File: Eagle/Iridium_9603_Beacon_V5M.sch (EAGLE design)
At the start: 103 parts, among them CON4 uFL, J1 SS4-10-3.50-X-D, Q1 DMG3415U-7, Q2 DMG3415U-7, Q3 DMG3415U-7, Q4 DMG3415U-7, Q5 2N2222, U1 MCP111T-240E/TT, U2 SPX3819-3.3, U3 LTC3225EDDB#TRMPBF, U4 MPL3115A2LGA8, U5 ATSAMD21G18_QFN, U6 MAX-M8, U7 LT1634-1,25BMCMS8, X1 32.768

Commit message: nr
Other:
- note added: "V5M: Double AA battery capacity Added mounting holes (M3)"
- note removed: "V5M: Double AA battery capacity"
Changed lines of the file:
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@@
 Added a pad for a battery power switch</text>
 <text x="157.48" y="149.86" size="2.54" layer="91" align="top-left">V5M:
-Double AA battery capacity</text>
+Double AA battery capacity
+Added mounting holes (M3)</text>
 </plain>
 <instances>

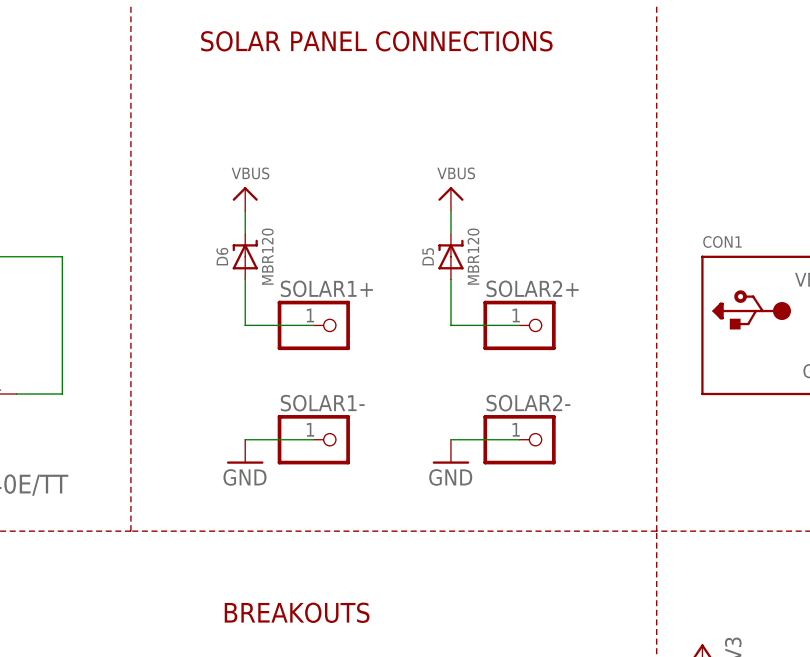
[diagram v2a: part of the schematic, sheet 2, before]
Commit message: removing backup eagle files, edits to V5M PCB board
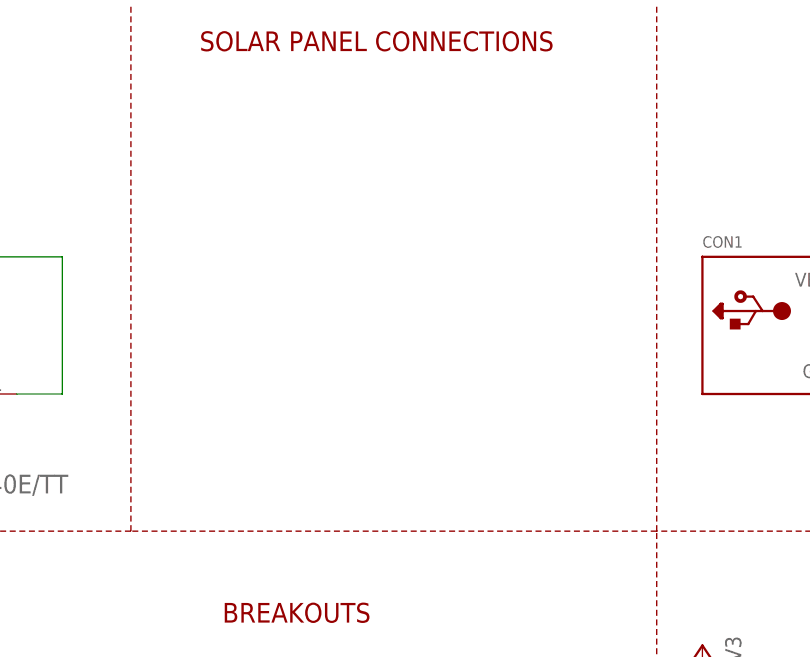
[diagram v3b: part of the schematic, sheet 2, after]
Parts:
- removed D5, D6: MBR120, microbuilder:DIODE-SCHOTTKYSOD-123
- removed SOLAR1+, SOLAR1-, SOLAR2+, SOLAR2-: (no value), adafruit:PINHD-1X1
- added FD3: FIDUCIAL1X2, SparkFun-Aesthetics:FIDUCIAL1X2
- added U$53: 7101K2AV2QE, argol-eagle-library:7101K2AV2QE
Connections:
- removed net N$14: D5.A, SOLAR2+.1
- removed net N$4: D6.A, SOLAR1+.1
- net GND: now also U$53.P$1; no longer SOLAR1-.1, SOLAR2-.1
- net N$15: now also U$53.P$2
- net VBUS: no longer D5.C, D6.C
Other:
- note added: "V5M: Double AA battery capacity Added mounting holes (M3) Added SPDT Switch for power Removed Solar Power connections"
- note removed: "Cut link if installing power switch"
- note removed: "V5M: Double AA battery capacity Added mounting holes (M3)"
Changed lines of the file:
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@@
 <layer number="59" name="tCarbon" color="7" fill="1" visible="no" active="no"/>
 <layer number="60" name="bCarbon" color="7" fill="1" visible="no" active="no"/>
+<layer number="88" name="SimResults" color="9" fill="1" visible="yes" active="yes"/>
+<layer number="89" name="SimProbes" color="9" fill="1" visible="yes" active="yes"/>
 <layer number="90" name="Modules" color="5" fill="1" visible="yes" active="yes"/>
 <layer number="91" name="Nets" color="2" fill="1" visible="yes" active="yes"/>
@@
 <part name="D3" library="microbuilder" deviceset="DIODE-SCHOTTKY" device="SOD-123" value="MBR120"/>
 <part name="D2" library="microbuilder" deviceset="DIODE-SCHOTTKY" device="SOD-123" value="MBR120"/>
-<part name="SOLAR1-" library="adafruit" library_urn="urn:adsk.eagle:library:420" deviceset="PINHD-1X1" device="" package3d_urn="urn:adsk.eagle:package:6240654/1"/>
-<part name="SOLAR2-" library="adafruit" library_urn="urn:adsk.eagle:library:420" deviceset="PINHD-1X1" device="" package3d_urn="urn:adsk.eagle:package:6240654/1"/>
-<part name="SOLAR1+" library="adafruit" library_urn="urn:adsk.eagle:library:420" deviceset="PINHD-1X1" device="" package3d_urn="urn:adsk.eagle:package:6240654/1"/>
-<part name="SOLAR2+" library="adafruit" library_urn="urn:adsk.eagle:library:420" deviceset="PINHD-1X1" device="" package3d_urn="urn:adsk.eagle:package:6240654/1"/>
-<part name="GND5" library="supply1" library_urn="urn:adsk.eagle:library:371" deviceset="GND" device=""/>
-<part name="GND6" library="supply1" library_urn="urn:adsk.eagle:library:371" deviceset="GND" device=""/>
-<part name="U$34" library="microbuilder" deviceset="VBUS" device=""/>
-<part name="D5" library="microbuilder" deviceset="DIODE-SCHOTTKY" device="SOD-123" value="MBR120"/>
-<part name="D6" library="microbuilder" deviceset="DIODE-SCHOTTKY" device="SOD-123" value="MBR120"/>
-<part name="U$2" library="microbuilder" deviceset="VBUS" device=""/>
 <part name="Q4" library="microbuilder" deviceset="MOSFET-P" device="WIDE" value="DMG3415U-7 "/>
 <part name="Q5" library="transistor" library_urn="urn:adsk.eagle:library:402" deviceset="*-NPN-" device="SOT23-BEC" package3d_urn="urn:adsk.eagle:package:28748/2" technology="MMBT2222ALT1" value="2N2222"/>
@@
 <part name="BAT5" library="SparkFun-Electromechanical" deviceset="BATTERY" device="KEYSTONE92"/>
 <part name="BAT6" library="SparkFun-Electromechanical" deviceset="BATTERY" device="KEYSTONE92"/>
+<part name="U$53" library="argol-eagle-library" deviceset="7101K2AV2QE" device=""/>
+<part name="FD3" library="SparkFun-Aesthetics" deviceset="FIDUCIAL" device="1X2"/>
 </parts>
 <sheets>
@@
 <text x="228.092" y="65.024" size="1.778" layer="91" align="bottom-center">Pads for battery
 power switch</text>
-<text x="189.484" y="64.516" size="1.778" layer="91" align="bottom-center">Cut link if installing
-power switch</text>
-<wire x1="207.772" y1="71.882" x2="205.232" y2="71.882" width="0.1524" layer="150"/>
-<wire x1="205.232" y1="71.882" x2="205.232" y2="61.722" width="0.1524" layer="150"/>
-<wire x1="205.232" y1="61.722" x2="207.772" y2="61.722" width="0.1524" layer="150"/>
 </plain>
 <instances>
@@
 <attribute name="VALUE" x="229.87" y="85.09" size="1.778" layer="96" rot="R270"/>
 </instance>
+<instance part="U$53" gate="G$1" x="193.04" y="71.12" smashed="yes" rot="R180"/>
+<instance part="FD3" gate="G$1" x="231.14" y="35.56" smashed="yes"/>
 </instances>
 <busses>
@@
 <segment>
 <pinref part="U$43" gate="G$1" pin="GND"/>
+<wire x1="218.44" y1="61.722" x2="218.44" y2="55.88" width="0.1524" layer="91"/>
 <pinref part="GND" gate="G$1" pin="1"/>
 <wire x1="210.312" y1="61.722" x2="218.44" y2="61.722" width="0.1524" layer="91"/>
-<wire x1="218.44" y1="61.722" x2="218.44" y2="55.88" width="0.1524" layer="91"/>
+<pinref part="U$53" gate="G$1" pin="P$1"/>
+<wire x1="180.34" y1="66.04" x2="180.34" y2="61.722" width="0.1524" layer="91"/>
+<wire x1="180.34" y1="61.722" x2="210.312" y2="61.722" width="0.1524" layer="91"/>
+<junction x="210.312" y="61.722"/>
 </segment>
 </net>
@@
 <wire x1="236.22" y1="76.2" x2="218.44" y2="76.2" width="0.1524" layer="91"/>
 <junction x="218.44" y="76.2"/>
+<junction x="210.312" y="71.882"/>
+<pinref part="U$53" gate="G$1" pin="P$2"/>
+<wire x1="210.312" y1="71.882" x2="210.312" y2="71.12" width="0.1524" layer="91"/>
+<wire x1="210.312" y1="71.12" x2="198.12" y2="71.12" width="0.1524" layer="91"/>
 </segment>
 </net>
@@
 <attribute name="VALUE" x="30.48" y="142.24" size="1.016" layer="96" font="vector" ratio="15" rot="R90" align="center"/>
 </instance>
-<instance part="SOLAR1-" gate="G$1" x="180.34" y="127" smashed="yes">
-<attribute name="NAME" x="173.99" y="130.175" size="1.778" layer="95"/>
-<attribute name="VALUE" x="173.99" y="121.92" size="1.778" layer="96"/>
-</instance>
-<instance part="SOLAR2-" gate="G$1" x="203.2" y="127" smashed="yes">
-<attribute name="NAME" x="196.85" y="130.175" size="1.778" layer="95"/>
-<attribute name="VALUE" x="196.85" y="121.92" size="1.778" layer="96"/>
-</instance>
-<instance part="SOLAR1+" gate="G$1" x="180.34" y="139.7" smashed="yes">
-<attribute name="NAME" x="173.99" y="142.875" size="1.778" layer="95"/>
-<attribute name="VALUE" x="173.99" y="134.62" size="1.778" layer="96"/>
-</instance>
-<instance part="SOLAR2+" gate="G$1" x="203.2" y="139.7" smashed="yes">
-<attribute name="NAME" x="196.85" y="142.875" size="1.778" layer="95"/>
-<attribute name="VALUE" x="196.85" y="134.62" size="1.778" layer="96"/>
-</instance>
-<instance part="GND5" gate="1" x="170.18" y="124.46" smashed="yes">
-<attribute name="VALUE" x="167.64" y="121.92" size="1.778" layer="96"/>
-</instance>
-<instance part="GND6" gate="1" x="193.04" y="124.46" smashed="yes">
-<attribute name="VALUE" x="190.5" y="121.92" size="1.778" layer="96"/>
-</instance>
-<instance part="U$34" gate="G$1" x="193.04" y="154.94" smashed="yes">
-<attribute name="VALUE" x="191.516" y="155.956" size="1.27" layer="96"/>
-</instance>
-<instance part="D5" gate="G$1" x="193.04" y="147.32" smashed="yes" rot="R90">
-<attribute name="NAME" x="190.5" y="147.32" size="1.27" layer="95" rot="R90" align="center"/>
-<attribute name="VALUE" x="195.54" y="147.32" size="1.27" layer="96" rot="R90" align="center"/>
-</instance>
-<instance part="D6" gate="G$1" x="170.18" y="147.32" smashed="yes" rot="R90">
-<attribute name="NAME" x="167.64" y="147.32" size="1.27" layer="95" rot="R90" align="center"/>
-<attribute name="VALUE" x="172.68" y="147.32" size="1.27" layer="96" rot="R90" align="center"/>
-</instance>
-<instance part="U$2" gate="G$1" x="170.18" y="154.94" smashed="yes">
-<attribute name="VALUE" x="168.656" y="155.956" size="1.27" layer="96"/>
-</instance>
 <instance part="RST" gate="G$1" x="208.28" y="91.44" smashed="yes">
 <attribute name="NAME" x="201.93" y="94.615" size="1.778" layer="95"/>
@@
 <pinref part="GND9" gate="1" pin="GND"/>
 <wire x1="223.52" y1="53.34" x2="223.52" y2="48.26" width="0.1524" layer="91"/>
-</segment>
-<segment>
-<pinref part="SOLAR1-" gate="G$1" pin="1"/>
-<pinref part="GND5" gate="1" pin="GND"/>
-<wire x1="177.8" y1="127" x2="170.18" y2="127" width="0.1524" layer="91"/>
-</segment>
-<segment>
-<pinref part="SOLAR2-" gate="G$1" pin="1"/>
-<pinref part="GND6" gate="1" pin="GND"/>
-<wire x1="200.66" y1="127" x2="193.04" y2="127" width="0.1524" layer="91"/>
 </segment>
 </net>
@@
 <wire x1="243.84" y1="152.4" x2="243.84" y2="157.48" width="0.1524" layer="91"/>
 </segment>
-<segment>
-<pinref part="D5" gate="G$1" pin="C"/>
-<pinref part="U$34" gate="G$1" pin="VBUS"/>
-<wire x1="193.04" y1="149.86" x2="193.04" y2="152.4" width="0.1524" layer="91"/>
-</segment>
-<segment>
-<pinref part="D6" gate="G$1" pin="C"/>
-<pinref part="U$2" gate="G$1" pin="VBUS"/>
-<wire x1="170.18" y1="149.86" x2="170.18" y2="152.4" width="0.1524" layer="91"/>
-</segment>
 </net>
 <net name="VBAT" class="0">
@@
 <wire x1="241.3" y1="144.78" x2="243.84" y2="144.78" width="0.1524" layer="91"/>
 <wire x1="243.84" y1="144.78" x2="243.84" y2="147.32" width="0.1524" layer="91"/>
-</segment>
-</net>
-<net name="N$14" class="0">
-<segment>
-<pinref part="SOLAR2+" gate="G$1" pin="1"/>
-<pinref part="D5" gate="G$1" pin="A"/>
-<wire x1="200.66" y1="139.7" x2="193.04" y2="139.7" width="0.1524" layer="91"/>
-<wire x1="193.04" y1="139.7" x2="193.04" y2="144.78" width="0.1524" layer="91"/>
-</segment>
-</net>
-<net name="N$4" class="0">
-<segment>
-<pinref part="SOLAR1+" gate="G$1" pin="1"/>
-<wire x1="177.8" y1="139.7" x2="170.18" y2="139.7" width="0.1524" layer="91"/>
-<pinref part="D6" gate="G$1" pin="A"/>
-<wire x1="170.18" y1="139.7" x2="170.18" y2="144.78" width="0.1524" layer="91"/>
 </segment>
 </net>
@@
 <text x="157.48" y="149.86" size="2.54" layer="91" align="top-left">V5M:
 Double AA battery capacity
-Added mounting holes (M3)</text>
+Added mounting holes (M3)
+Added SPDT Switch for power
+Removed Solar Power connections</text>
 </plain>
 <instances>

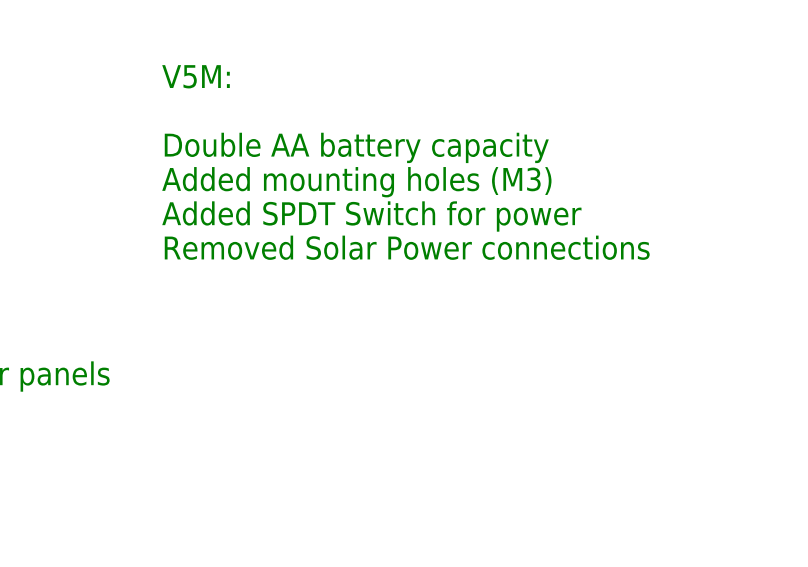
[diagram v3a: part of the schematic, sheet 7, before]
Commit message: Clean version of board modifications.  Extra batteries, switch added.  Reset button flipped to bottom.  Moved USB port.  NO EXTRA serial port yet.
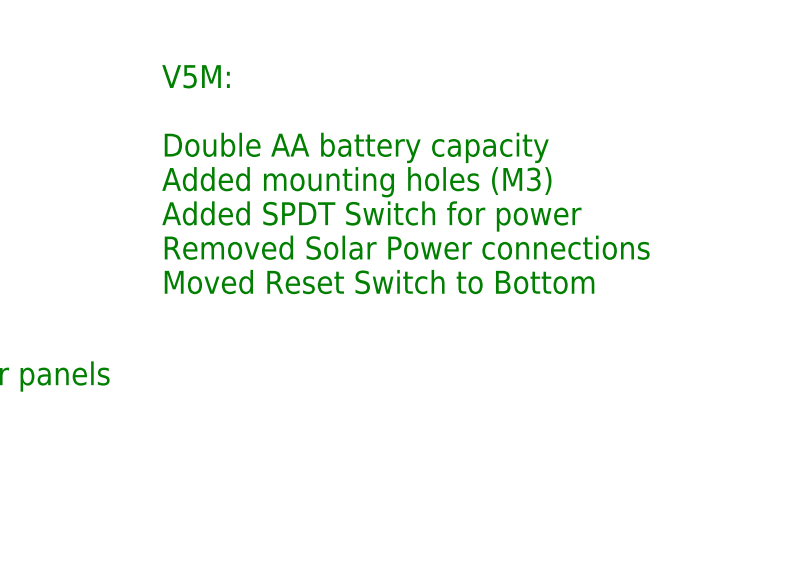
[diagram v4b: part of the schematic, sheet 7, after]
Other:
- note added: "V5M: Double AA battery capacity Added mounting holes (M3) Added SPDT Switch for power Removed Solar Power connections Moved Reset Switch to Bottom"
- note removed: "V5M: Double AA battery capacity Added mounting holes (M3) Added SPDT Switch for power Removed Solar Power connections"
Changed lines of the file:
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@@
 Added mounting holes (M3)
 Added SPDT Switch for power
-Removed Solar Power connections</text>
+Removed Solar Power connections
+Moved Reset Switch to Bottom</text>
 </plain>
 <instances>
